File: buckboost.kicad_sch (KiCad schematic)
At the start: 15 parts, among them Q1 AO3401A, Q2 AO3401A, Q3 AO3400A, Q4 AO3400A, U4 IRS2003, U5 IRS2003

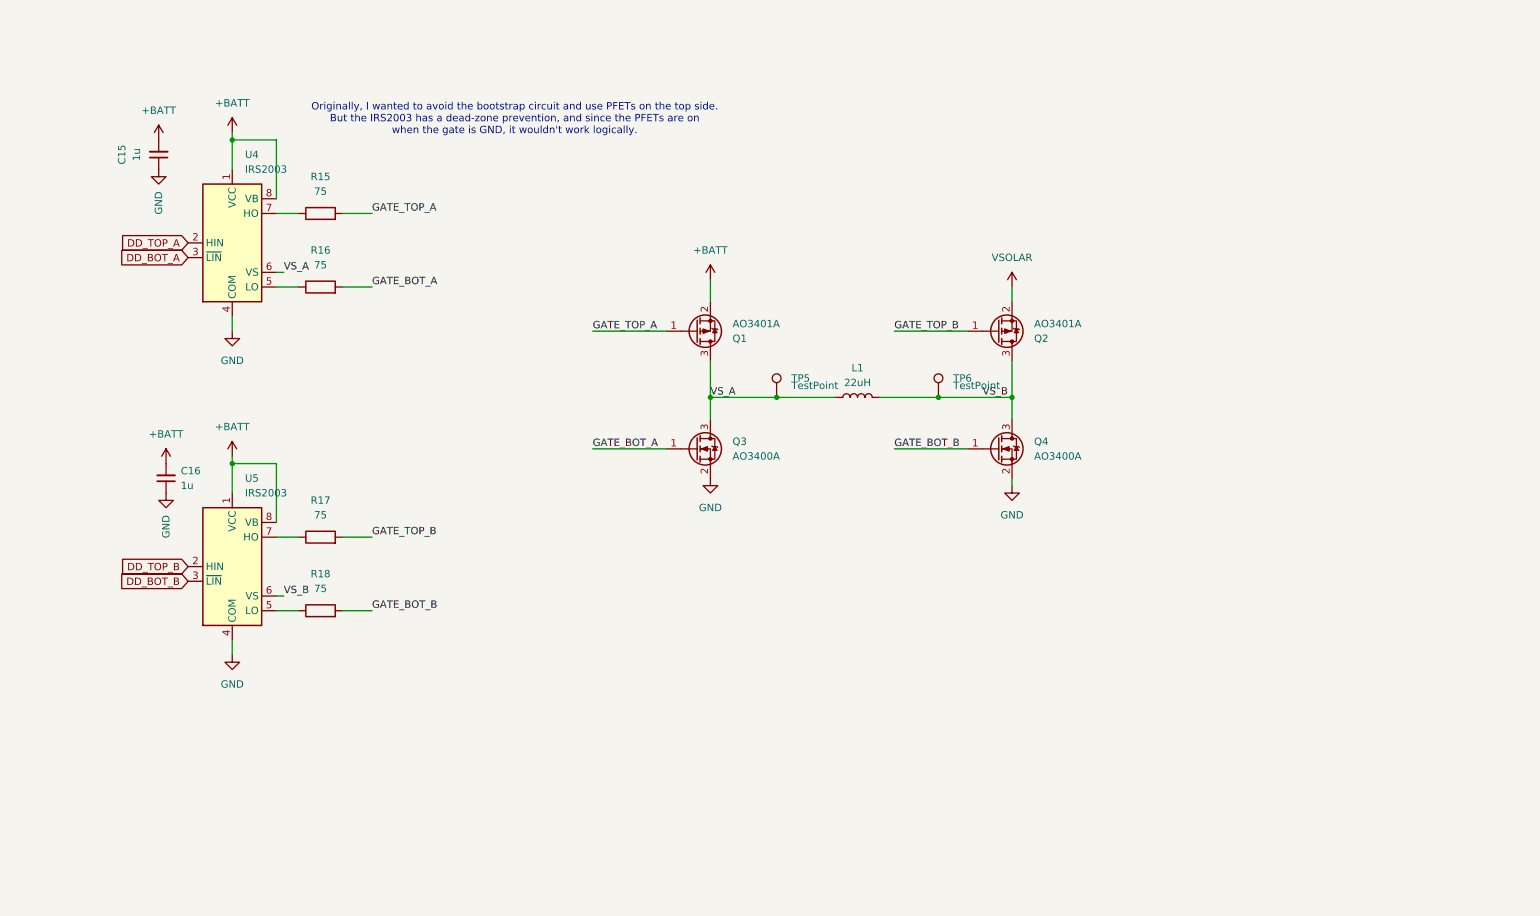
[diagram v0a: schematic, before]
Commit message: N fets
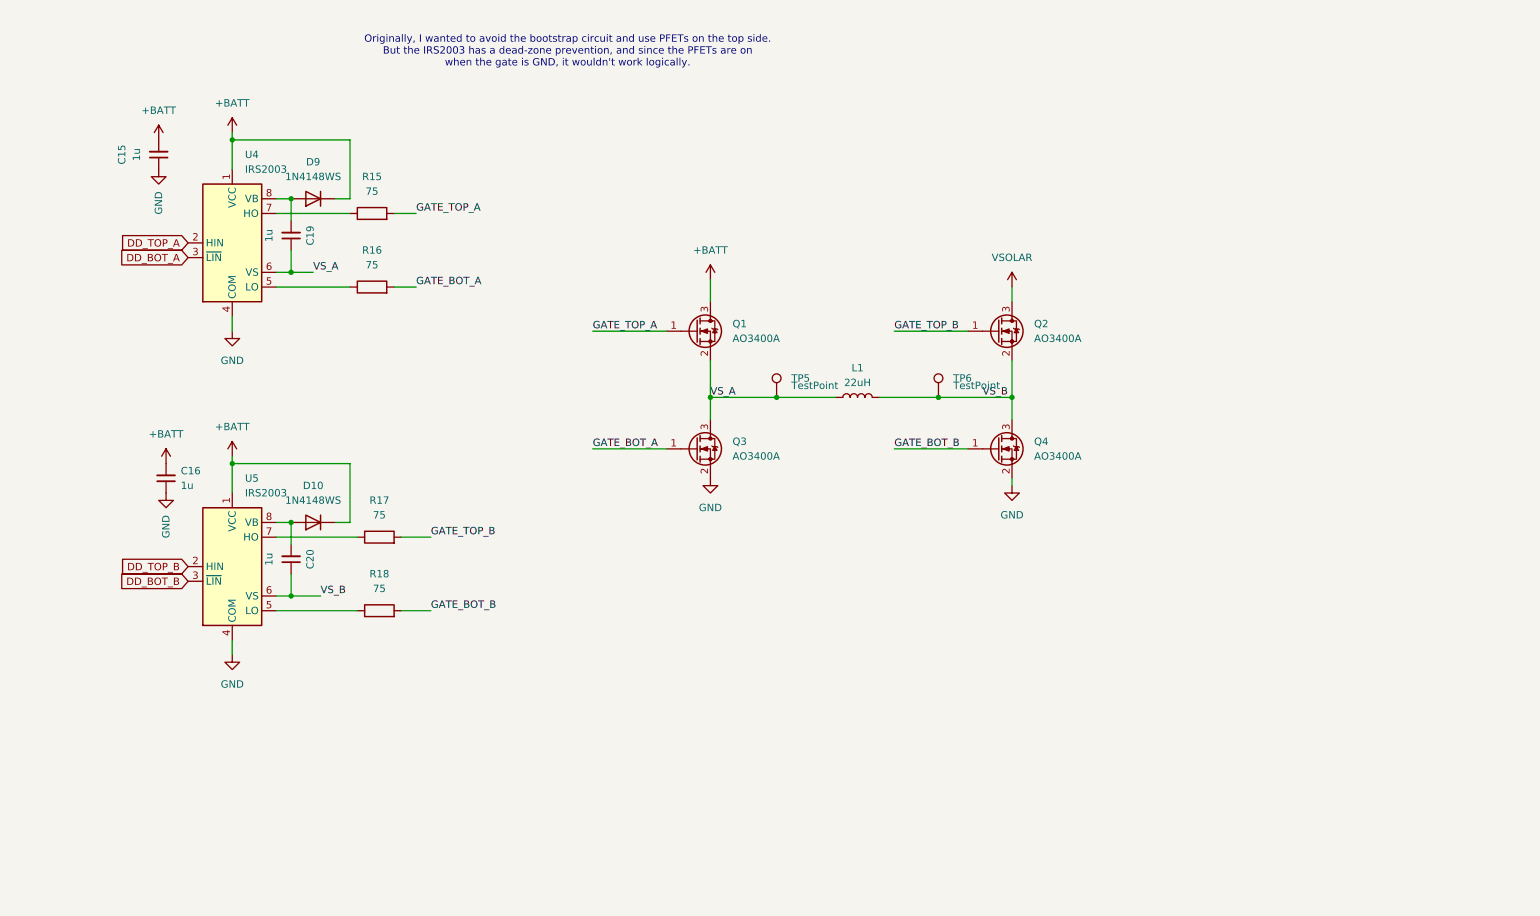
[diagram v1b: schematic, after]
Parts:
- removed Q1, Q2: AO3401A, Package_TO_SOT_SMD:SOT-23, symbol Transistor_FET:AO3401A
- added C19, C20: 1u, Capacitor_SMD:C_0603_1608Metric, symbol Device:C_Small
- added D10, D9: 1N4148WS, Diode_SMD:D_SOD-323, symbol Diode:1N4148WS
- added Q1, Q2: AO3400A, Package_TO_SOT_SMD:SOT-23, symbol Transistor_FET:AO3400A
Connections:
- net +BATT: now also D10.1 (K), D9.1 (K), Q1.3 (D); no longer U4.8 (VB), U5.8 (VB)
- net GATE_TOP_A: now also Q1.1 (G)
- net GATE_TOP_B: now also Q2.1 (G)
- net VSOLAR: now also Q2.3 (D)
- net VS_A: now also C19.1, Q1.2 (S)
- net VS_B: now also C20.1, Q2.2 (S)
- new net: C20.2, D10.2 (A), U5.8 (VB)
- new net: C19.2, D9.2 (A), U4.8 (VB)
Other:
- moved on the sheet: R15, R16, R17, R18

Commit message: Adding a few notes, adding detection on solar and uart plugs
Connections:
- net +BATT: now also D10.2 (A), D9.2 (A); no longer D10.1 (K), D9.1 (K)
- net at C20.2, U5.8 (VB): now also D10.1 (K); no longer D10.2 (A)
- net at C19.2, U4.8 (VB): now also D9.1 (K); no longer D9.2 (A)
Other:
- moved on the sheet: D10, D9
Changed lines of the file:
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@@
 	(symbol
 		(lib_id "Diode:1N4148WS")
-		(at 76.2 106.68 180)
-		(unit 1)
-		(exclude_from_sim no)
-		(in_bom yes)
-		(on_board yes)
-		(dnp no)
-		(fields_autoplaced yes)
+		(at 76.2 106.68 0)
+		(mirror x)
+		(unit 1)
+		(exclude_from_sim no)
+		(in_bom yes)
+		(on_board yes)
+		(dnp no)
 		(property "Reference" "D10"
 			(at 76.2 100.33 0)
@@
 	(symbol
 		(lib_id "Diode:1N4148WS")
-		(at 76.2 50.8 180)
-		(unit 1)
-		(exclude_from_sim no)
-		(in_bom yes)
-		(on_board yes)
-		(dnp no)
-		(fields_autoplaced yes)
+		(at 76.2 50.8 0)
+		(mirror x)
+		(unit 1)
+		(exclude_from_sim no)
+		(in_bom yes)
+		(on_board yes)
+		(dnp no)
 		(property "Reference" "D9"
 			(at 76.2 44.45 0)

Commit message: Adding new ST driver, protecting uart input
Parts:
- removed U4, U5: IRS2003, Package_SO:SOIC-8_3.9x4.9mm_P1.27mm, symbol Driver_FET:IRS2003
- added U6: L6388E, Package_SO:SO-8_3.9x4.9mm_P1.27mm, symbol JakeLib:L6388E
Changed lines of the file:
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@@
+	)
+	(symbol
+		(lib_id "JakeLib:L6388E")
+		(at 31.75 78.74 0)
+		(unit 1)
+		(exclude_from_sim no)
+		(in_bom yes)
+		(on_board yes)
+		(dnp no)
+		(fields_autoplaced yes)
+		(property "Reference" "U6"
+			(at 32.385 64.77 0)
+			(effects
+				(font
+					(size 1.27 1.27)
+				)
+			)
+		)
+		(property "Value" "L6388E"
+			(at 32.385 67.31 0)
+			(effects
+				(font
+					(size 1.27 1.27)
+				)
+			)
+		)
+		(property "Footprint" "Package_SO:SO-8_3.9x4.9mm_P1.27mm"
+			(at 29.464 87.122 0)
+			(effects
+				(font
+					(size 1.27 1.27)
+				)
+				(hide yes)
+			)
+		)
+		(property "Datasheet" "https://www.st.com/resource/en/datasheet/l6388e.pdf"
+			(at 31.75 85.09 0)
+			(effects
+				(font
+					(size 1.27 1.27)
+				)
+				(hide yes)
+			)
+		)
+		(property "Description" ""
+			(at 31.75 78.74 0)
+			(effects
+				(font
+					(size 1.27 1.27)
+				)
+				(hide yes)
+			)
+		)
+		(pin "1"
+		)
+		(pin "4"
+		)
+		(pin "6"
+		)
+		(pin "3"
+		)
+		(pin "5"
+		)
+		(pin "8"
+		)
+		(pin "7"
+		)
+		(pin "2"
+		)
+		(instances
+			(project "JPBms2"
+				(path "/d86e471c-a8be-422d-a5d1-5a4699b7b766/0f5ad211-c4ad-40eb-a8ac-82970ee8fac9"
+					(reference "U6")
+					(unit 1)
+				)
+			)
+		)
 	)
 	(symbol
@@
 	)
 	(symbol
-		(lib_id "Driver_FET:IRS2003")
-		(at 62.23 58.42 0)
-		(unit 1)
-		(exclude_from_sim no)
-		(in_bom yes)
-		(on_board yes)
-		(dnp no)
-		(fields_autoplaced yes)
-		(property "Reference" "U4"
-			(at 64.4241 43.18 0)
-			(effects
-				(font
-					(size 1.27 1.27)
-				)
-				(justify left)
-			)
-		)
-		(property "Value" "IRS2003"
-			(at 64.4241 45.72 0)
-			(effects
-				(font
-					(size 1.27 1.27)
-				)
-				(justify left)
-			)
-		)
-		(property "Footprint" "Package_SO:SOIC-8_3.9x4.9mm_P1.27mm"
-			(at 62.23 58.42 0)
-			(effects
-				(font
-					(size 1.27 1.27)
-					(italic yes)
-				)
-				(hide yes)
-			)
-		)
-		(property "Datasheet" "https://www.infineon.com/dgdl/irs2003pbf.pdf?fileId=5546d462533600a401535675afec2780"
-			(at 62.23 58.42 0)
-			(effects
-				(font
-					(size 1.27 1.27)
-				)
-				(hide yes)
-			)
-		)
-		(property "Description" "Half-Bridge Driver, 200V, 290/600mA, PDIP-8/SOIC-8"
-			(at 62.23 58.42 0)
-			(effects
-				(font
-					(size 1.27 1.27)
-				)
-				(hide yes)
-			)
-		)
-		(property "LCSC_Code" "C40009"
-			(at 62.23 58.42 0)
-			(effects
-				(font
-					(size 1.27 1.27)
-				)
-				(hide yes)
-			)
-		)
-		(pin "7"
-		)
-		(pin "8"
-		)
-		(pin "1"
-		)
-		(pin "3"
-		)
-		(pin "5"
-		)
-		(pin "6"
-		)
-		(pin "2"
-		)
-		(pin "4"
-		)
-		(instances
-			(project "JPBms2"
-				(path "/d86e471c-a8be-422d-a5d1-5a4699b7b766/0f5ad211-c4ad-40eb-a8ac-82970ee8fac9"
-					(reference "U4")
-					(unit 1)
-				)
-			)
-		)
-	)
-	(symbol
 		(lib_id "Device:C_Small")
 		(at 72.39 57.15 180)
@@
 					(unit 1)
 				)
-			)
-		)
-	)
-	(symbol
-		(lib_id "Driver_FET:IRS2003")
-		(at 62.23 114.3 0)
-		(unit 1)
-		(exclude_from_sim no)
-		(in_bom yes)
-		(on_board yes)
-		(dnp no)
-		(fields_autoplaced yes)
-		(property "Reference" "U5"
-			(at 64.4241 99.06 0)
-			(effects
-				(font
-					(size 1.27 1.27)
-				)
-				(justify left)
-			)
-		)
-		(property "Value" "IRS2003"
-			(at 64.4241 101.6 0)
-			(effects
-				(font
-					(size 1.27 1.27)
-				)
-				(justify left)
-			)
-		)
-		(property "Footprint" "Package_SO:SOIC-8_3.9x4.9mm_P1.27mm"
-			(at 62.23 114.3 0)
-			(effects
-				(font
-					(size 1.27 1.27)
-					(italic yes)
-				)
-				(hide yes)
-			)
-		)
-		(property "Datasheet" "https://www.infineon.com/dgdl/irs2003pbf.pdf?fileId=5546d462533600a401535675afec2780"
-			(at 62.23 114.3 0)
-			(effects
-				(font
-					(size 1.27 1.27)
-				)
-				(hide yes)
-			)
-		)
-		(property "Description" "Half-Bridge Driver, 200V, 290/600mA, PDIP-8/SOIC-8"
-			(at 62.23 114.3 0)
-			(effects
-				(font
-					(size 1.27 1.27)
-				)
-				(hide yes)
-			)
-		)
-		(property "LCSC_Code" "C40009"
-			(at 62.23 114.3 0)
-			(effects
-				(font
-					(size 1.27 1.27)
-				)
-				(hide yes)
-			)
-		)
-		(pin "7"
-		)
-		(pin "8"
-		)
-		(pin "1"
-		)
-		(pin "3"
-		)
-		(pin "5"
-		)
-		(pin "6"
-		)
-		(pin "2"
-		)
-		(pin "4"
-		)
-		(instances
-			(project "JPBms2"
-				(path "/d86e471c-a8be-422d-a5d1-5a4699b7b766/0f5ad211-c4ad-40eb-a8ac-82970ee8fac9"
-					(reference "U5")
-					(unit 1)
-				)

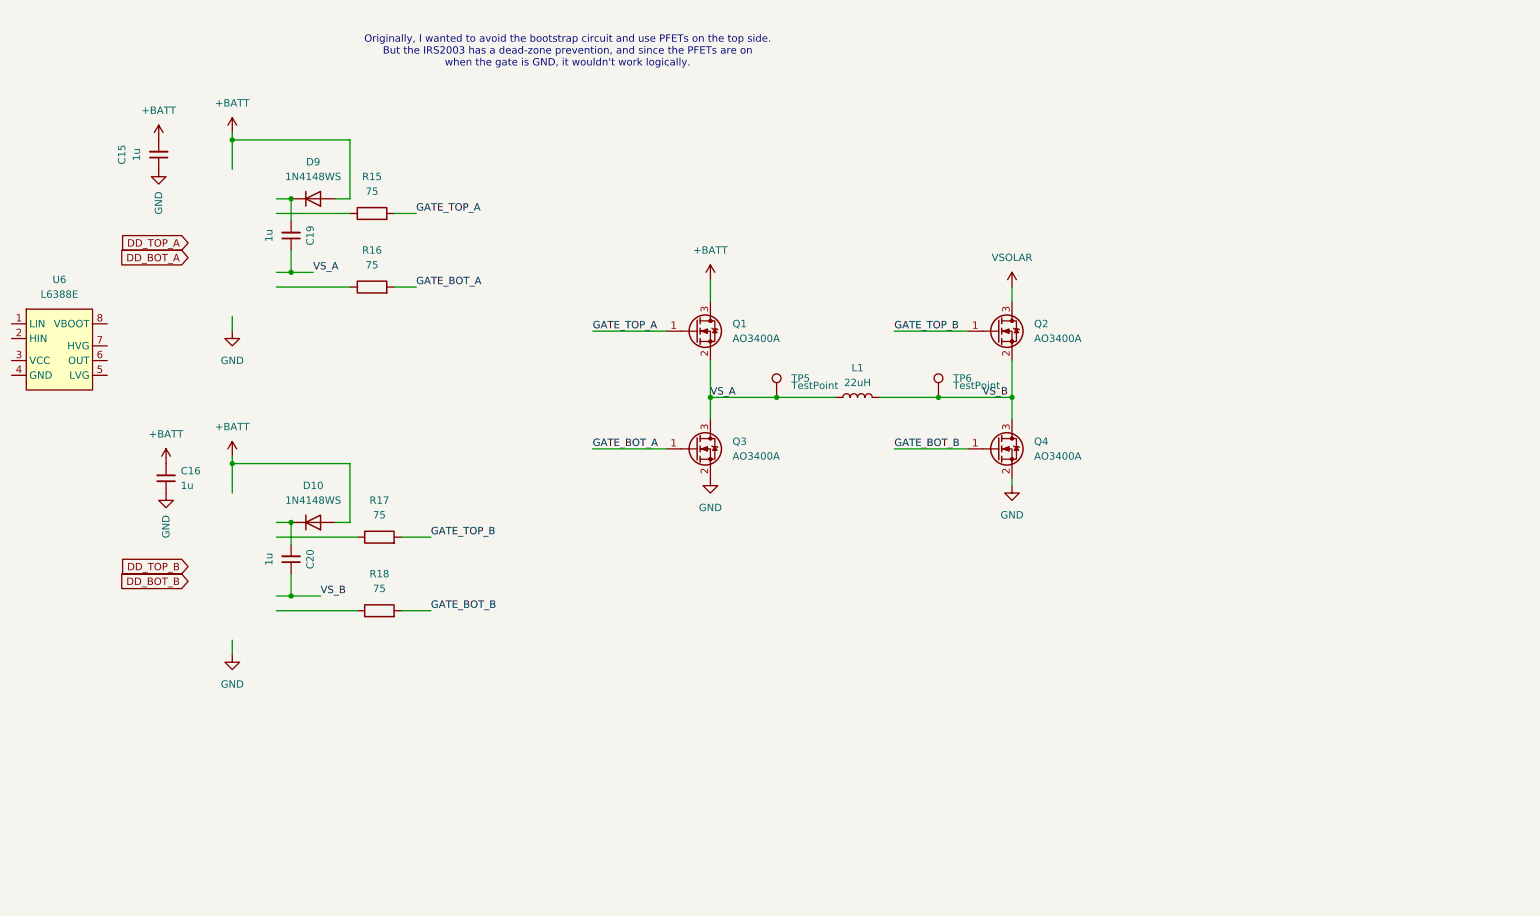
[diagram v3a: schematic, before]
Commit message: Taking notes, doing some final adjustments to RC filter values
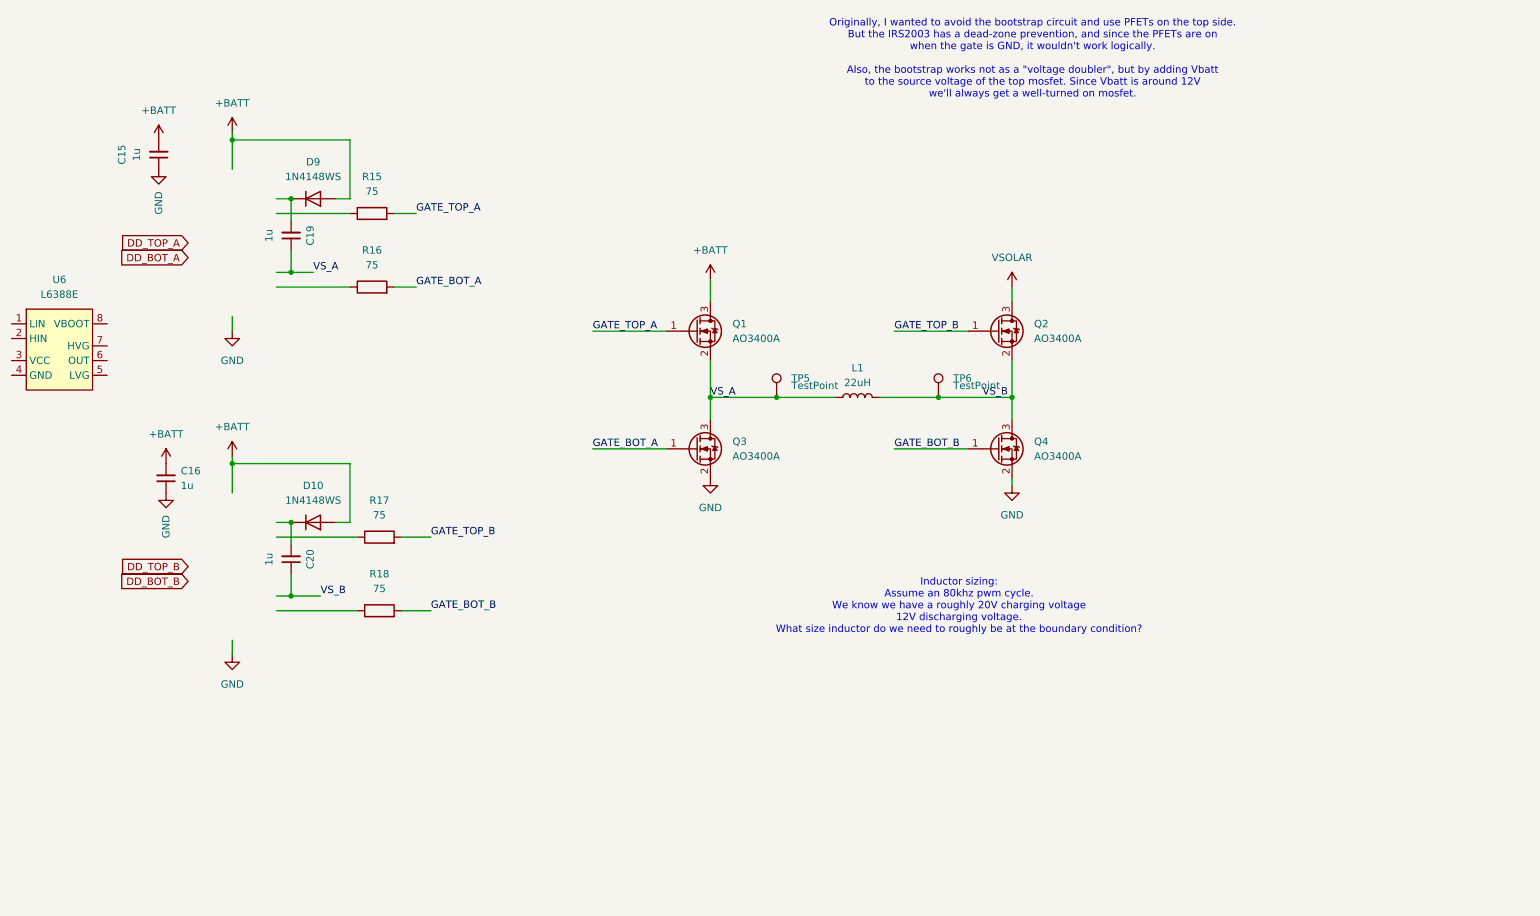
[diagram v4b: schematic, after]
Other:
- note added: "Inductor sizing: Assume an 80khz pwm cycle. We know we have a roughly 20V charging voltage 12V discharging voltage. What size inductor do we need to roughly be at the boundary condition?"
- note added: "Originally, I wanted to avoid the bootstrap circuit and use PFETs on the top side. But the IRS2003 has a dead-zone prevention, and since the PFETs are on when the gate is GND, it wouldn't work logically. Also, the bootstrap works not as a "voltage doubler", but by adding Vbatt to the source voltage of the top mosfet. Since Vbatt is around 12V we'll always get a well-turned on mosfet."
- note removed: "Originally, I wanted to avoid the bootstrap circuit and use PFETs on the top side. But the IRS2003 has a dead-zone prevention, and since the PFETs are on when the gate is GND, it wouldn't work logically."
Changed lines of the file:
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@@
 		)
 	)
-	(text "Originally, I wanted to avoid the bootstrap circuit and use PFETs on the top side.\nBut the IRS2003 has a dead-zone prevention, and since the PFETs are on \nwhen the gate is GND, it wouldn't work logically."
+	(text "Inductor sizing:\nAssume an 80khz pwm cycle.\nWe know we have a roughly 20V charging voltage\n12V discharging voltage.\nWhat size inductor do we need to roughly be at the boundary condition?"
 		(exclude_from_sim no)
-		(at 120.142 25.4 0)
+		(at 187.706 121.158 0)
 		(effects
 			(font
+				(size 1.27 1.27)
+			)
+		)
+	)
+	(text "Originally, I wanted to avoid the bootstrap circuit and use PFETs on the top side.\nBut the IRS2003 has a dead-zone prevention, and since the PFETs are on \nwhen the gate is GND, it wouldn't work logically.\n\nAlso, the bootstrap works not as a \"voltage doubler\", but by adding Vbatt\nto the source voltage of the top mosfet. Since Vbatt is around 12V\nwe'll always get a well-turned on mosfet."
+		(exclude_from_sim no)
+		(at 200.406 26.67 0)
+		(effects
+			(font
